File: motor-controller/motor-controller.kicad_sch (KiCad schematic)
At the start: 14 parts, among them Q1 IRFZ44, Q2 IRFZ44, Q3 IRFZ44, Q4 IRFZ44, Q5 VN2222L, Q6 VN2222L, U1 MCT6, U2 LT1161

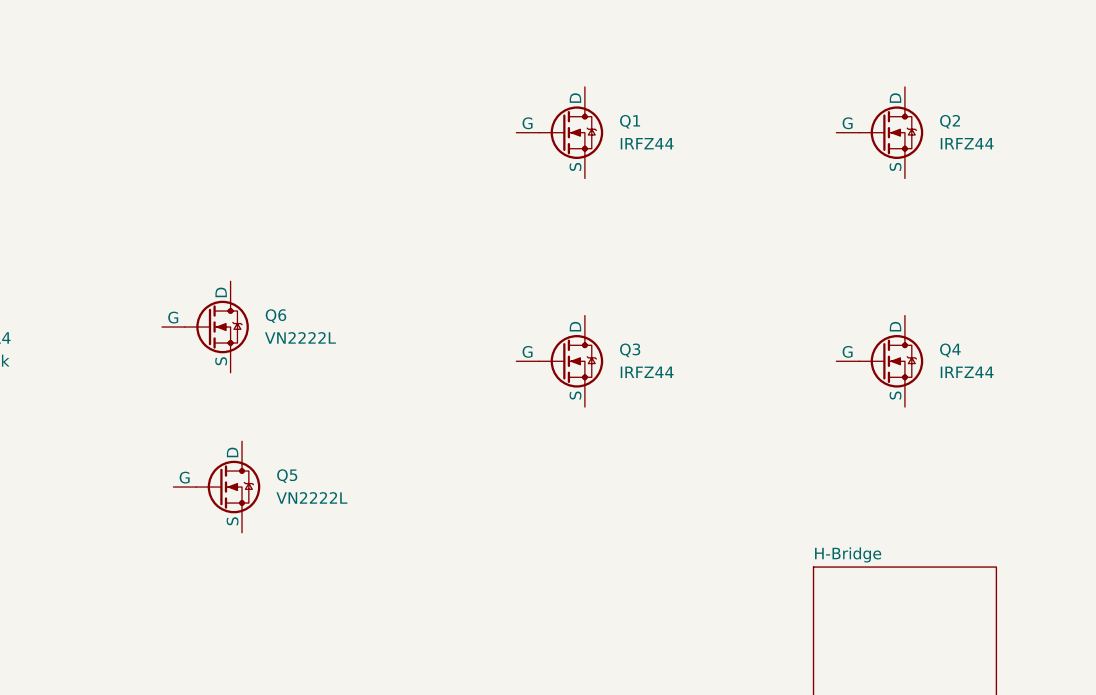
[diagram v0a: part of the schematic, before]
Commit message: Create H-Bridge schematic
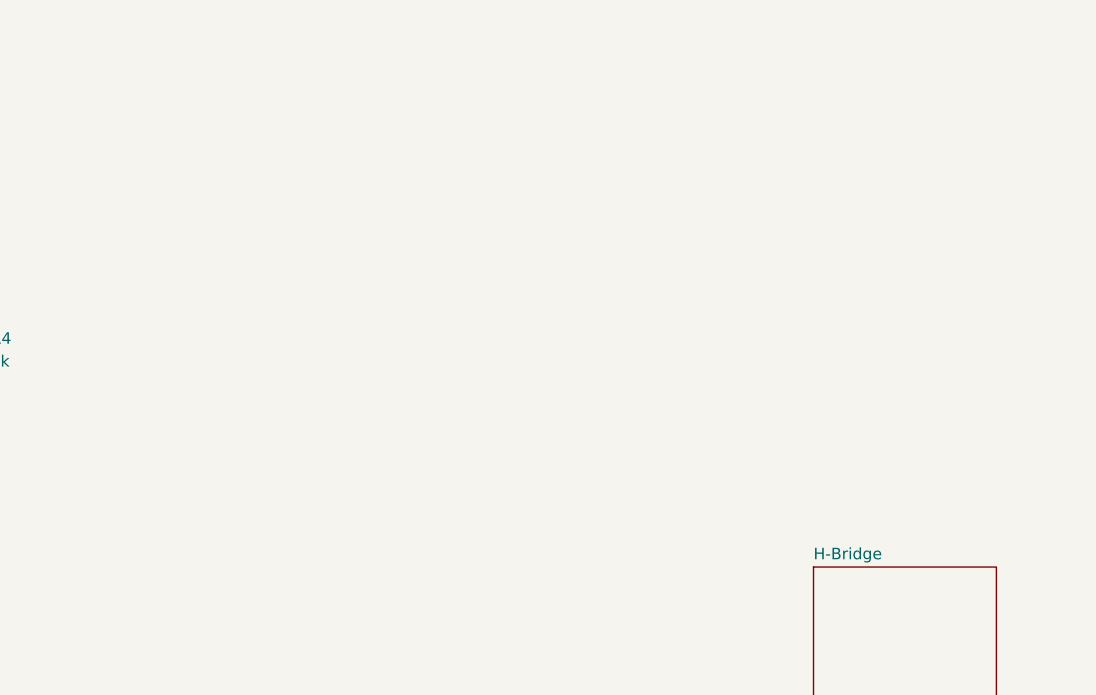
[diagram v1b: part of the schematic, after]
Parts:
- removed Q1, Q2, Q3, Q4: IRFZ44, Package_TO_SOT_THT:TO-220-3_Vertical, symbol GS_Transistors:MOSFET_N-Ch_60V_48A_23mR
- removed Q5, Q6: VN2222L, Package_TO_SOT_THT:TO-92_Inline, symbol GS_Transistors:MOSFET_N-Ch_60V_0.23A_7500mR
- C1, C2: symbol Device:C -> GS_Capacitor_THT:C_THT_100nF
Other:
- company: (none) -> Team 5

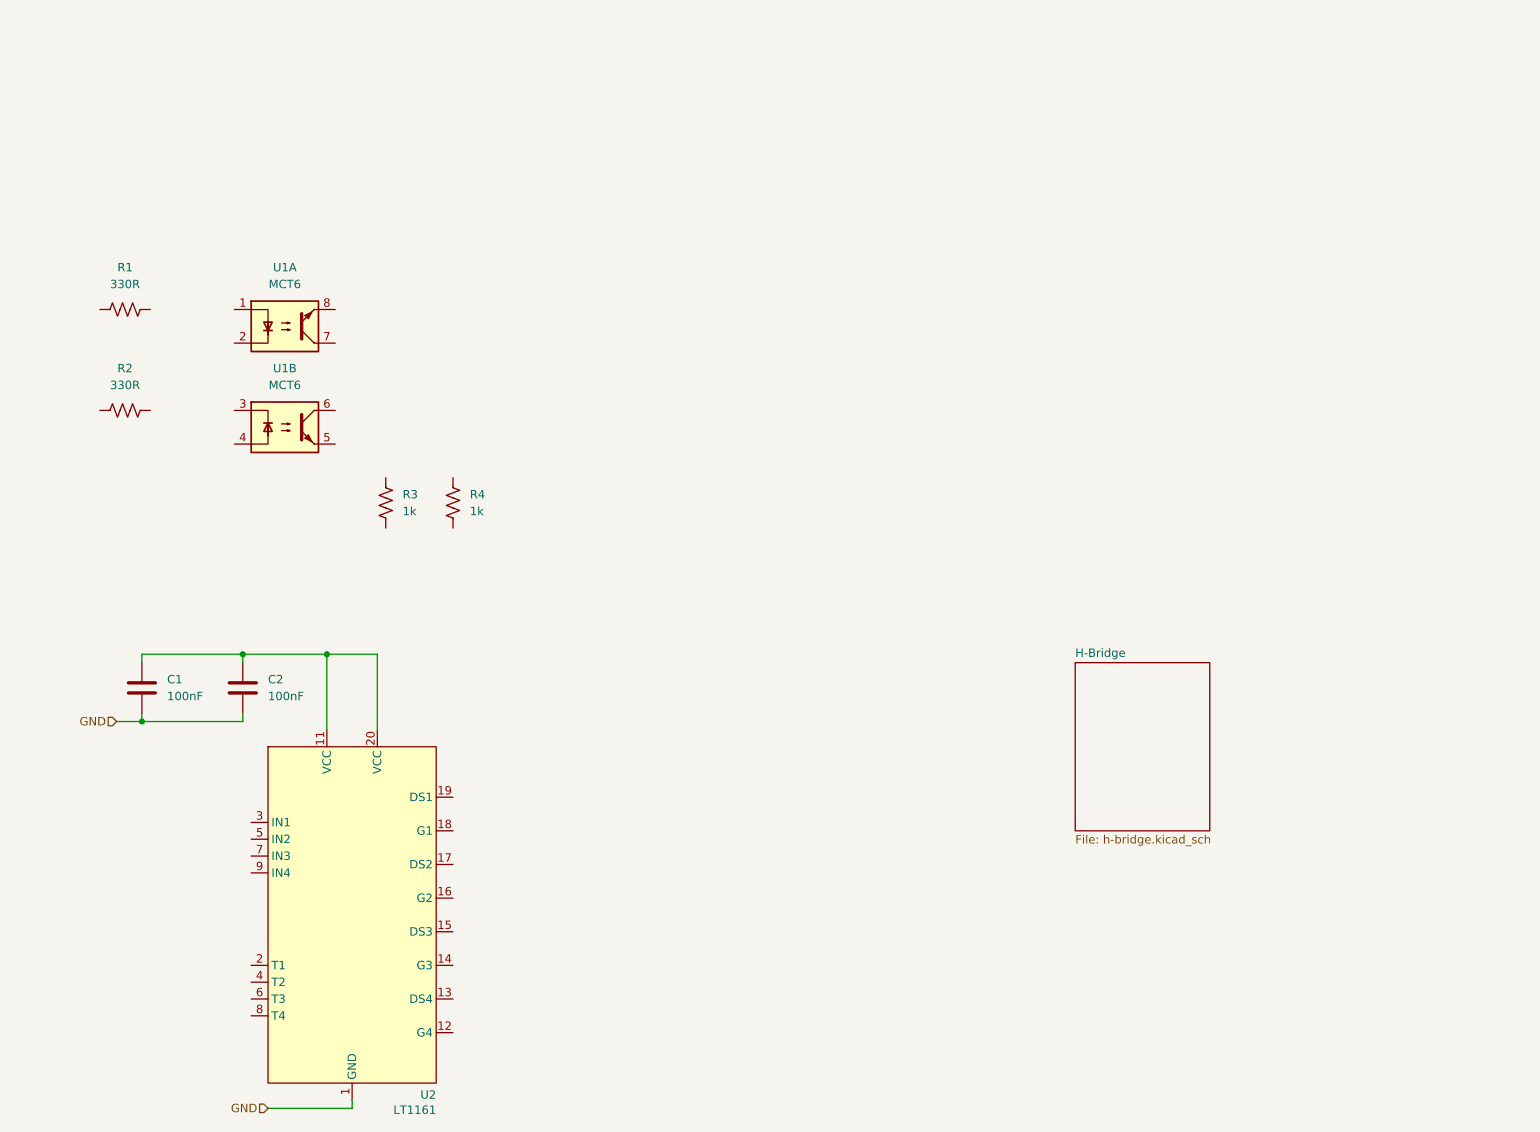
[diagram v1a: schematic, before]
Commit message: Finish optocoupler and gate-driver
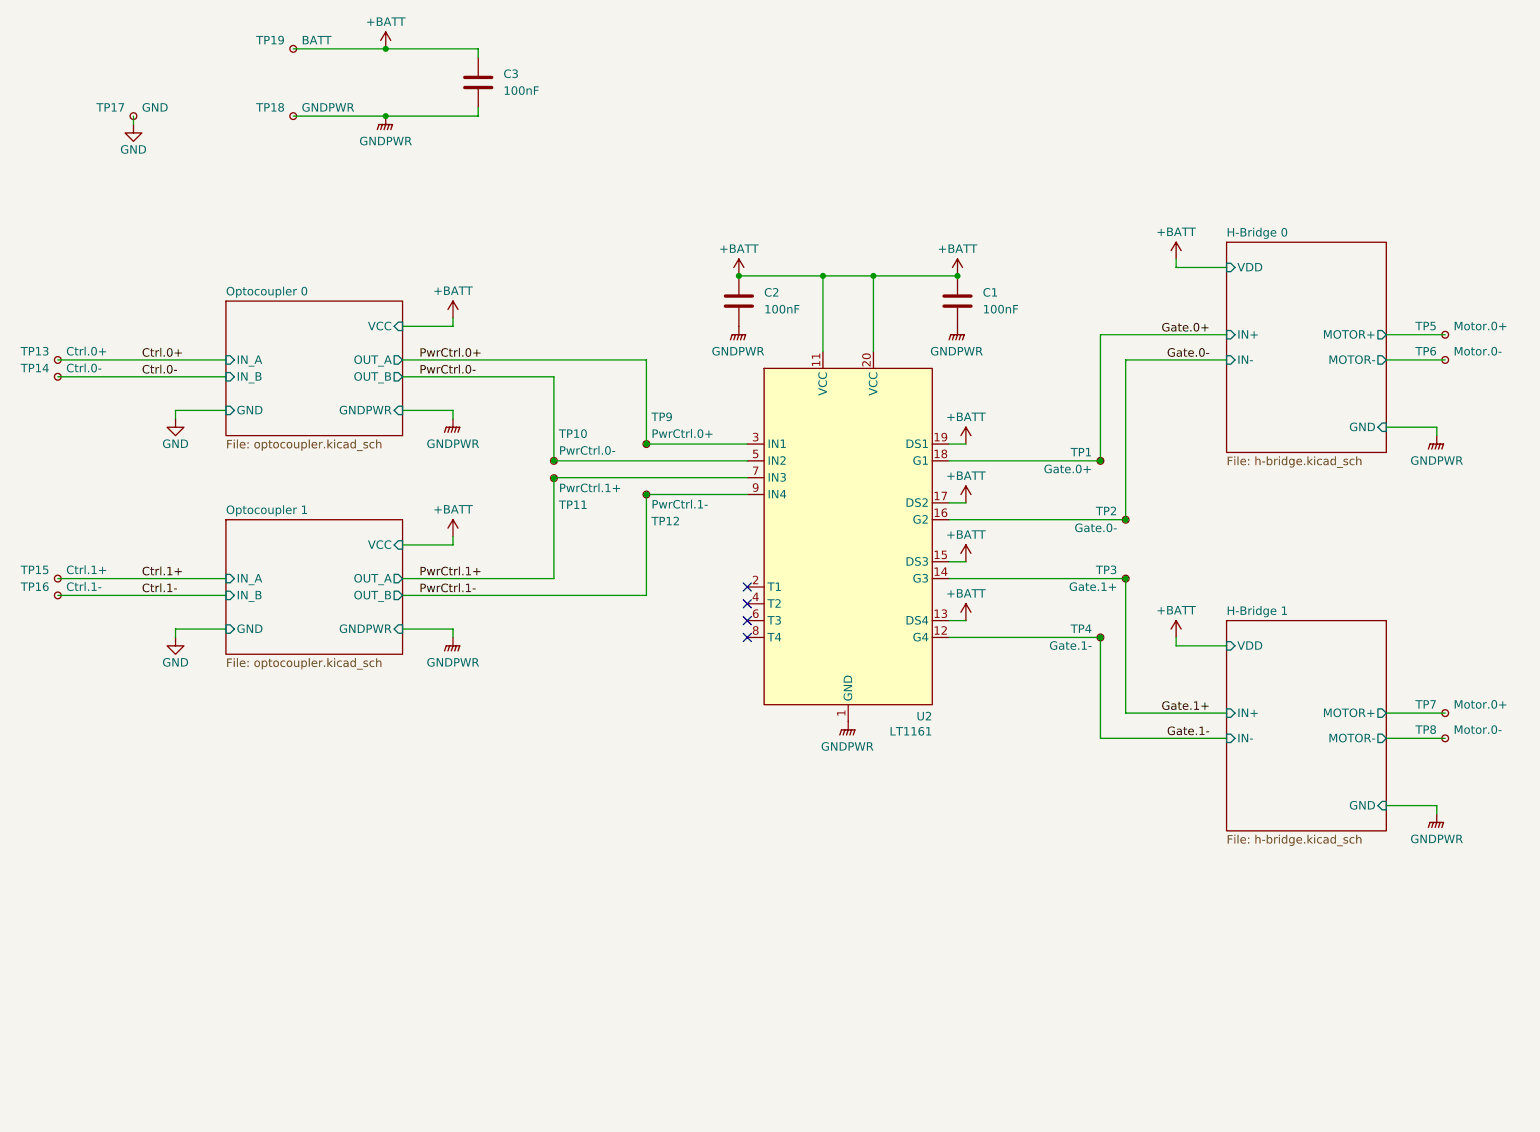
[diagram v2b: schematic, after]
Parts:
- removed R1, R2: 330R, Resistor_THT:R_Axial_DIN0309_L9.0mm_D3.2mm_P12.70mm_Horizontal, symbol Device:R_US
- removed R3, R4: 1k, Resistor_THT:R_Axial_DIN0309_L9.0mm_D3.2mm_P12.70mm_Horizontal, symbol Device:R_US
- removed U1: MCT6, Package_DIP:DIP-8_W7.62mm_LongPads, symbol GS_Optoelectronic:MCT6
- added C3: 100nF, Capacitor_THT:C_Disc_D3.0mm_W2.0mm_P2.50mm, symbol GS_Capacitor_THT:C_THT_100nF
- added TP1: Gate.0+, TestPoint:TestPoint_Pad_1.5x1.5mm, symbol Connector:TestPoint_Small
- added TP10: PwrCtrl.0-, TestPoint:TestPoint_Pad_1.5x1.5mm, symbol Connector:TestPoint_Small
- added TP11: PwrCtrl.1+, TestPoint:TestPoint_Pad_1.5x1.5mm, symbol Connector:TestPoint_Small
- added TP12: PwrCtrl.1-, TestPoint:TestPoint_Pad_1.5x1.5mm, symbol Connector:TestPoint_Small
- added TP13: Ctrl.0+, TestPoint:TestPoint_Pad_1.5x1.5mm, symbol Connector:TestPoint_Small
- added TP14: Ctrl.0-, TestPoint:TestPoint_Pad_1.5x1.5mm, symbol Connector:TestPoint_Small
- added TP15: Ctrl.1+, TestPoint:TestPoint_Pad_1.5x1.5mm, symbol Connector:TestPoint_Small
- added TP16: Ctrl.1-, TestPoint:TestPoint_Pad_1.5x1.5mm, symbol Connector:TestPoint_Small
- added TP17: GND, TestPoint:TestPoint_Pad_1.5x1.5mm, symbol Connector:TestPoint_Small
- added TP18: GNDPWR, TestPoint:TestPoint_Pad_1.5x1.5mm, symbol Connector:TestPoint_Small
- added TP19: BATT, TestPoint:TestPoint_Pad_1.5x1.5mm, symbol Connector:TestPoint_Small
- added TP2: Gate.0-, TestPoint:TestPoint_Pad_1.5x1.5mm, symbol Connector:TestPoint_Small
- added TP3: Gate.1+, TestPoint:TestPoint_Pad_1.5x1.5mm, symbol Connector:TestPoint_Small
- added TP4: Gate.1-, TestPoint:TestPoint_Pad_1.5x1.5mm, symbol Connector:TestPoint_Small
- added TP5, TP7: Motor.0+, TestPoint:TestPoint_Pad_1.5x1.5mm, symbol Connector:TestPoint_Small
- added TP6, TP8: Motor.0-, TestPoint:TestPoint_Pad_1.5x1.5mm, symbol Connector:TestPoint_Small
- added TP9: PwrCtrl.0+, TestPoint:TestPoint_Pad_1.5x1.5mm, symbol Connector:TestPoint_Small
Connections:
- net GND: now also C3.2, TP17.1, TP18.1
- net +BATT: now reaches C1.1, C2.1, U2.11 (VCC), U2.20 (VCC)
- net +BATT: now also U2.13 (DS4), U2.15 (DS3), U2.17 (DS2), U2.19 (DS1), C3.1, TP19.1
- net Gate.1-: now reaches U2.12 (G4)
- net Gate.1-: now also TP4.1
- net Gate.1+: now reaches U2.14 (G3)
- net Gate.1+: now also TP3.1
- net Gate.0-: now reaches U2.16 (G2)
- net Gate.0-: now also TP2.1
- net Gate.0+: now reaches U2.18 (G1)
- net Gate.0+: now also TP1.1
- net PwrCtrl.0+: now reaches U2.3 (IN1)
- net PwrCtrl.0+: now also TP9.1
- net PwrCtrl.0-: now reaches U2.5 (IN2)
- net PwrCtrl.0-: now also TP10.1
- net PwrCtrl.1+: now reaches U2.7 (IN3)
- net PwrCtrl.1+: now also TP11.1
- net PwrCtrl.1-: now reaches U2.9 (IN4)
- net PwrCtrl.1-: now also TP12.1
- new net Ctrl.0+: TP13.1
- new net Ctrl.0-: TP14.1
- new net Ctrl.1+: TP15.1
- new net Ctrl.1-: TP16.1
- new net H-Bridge 0/MOTOR+: TP5.1
- new net H-Bridge 0/MOTOR-: TP6.1
- new net H-Bridge 1/MOTOR+: TP7.1
- new net H-Bridge 1/MOTOR-: TP8.1
- no-connect marks 0 -> 4
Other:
- sheet H-Bridge renamed H-Bridge 1
- added sheet H-Bridge 0 (h-bridge.kicad_sch)
- added sheet Optocoupler 0 (optocoupler.kicad_sch)
- added sheet Optocoupler 1 (optocoupler.kicad_sch)
- sheet H-Bridge 1 ports: added GND, IN+, IN-, MOTOR+, MOTOR-, VDD; removed none
- title: (none) -> Motor Controller
- moved on the sheet: C1, C2, U2

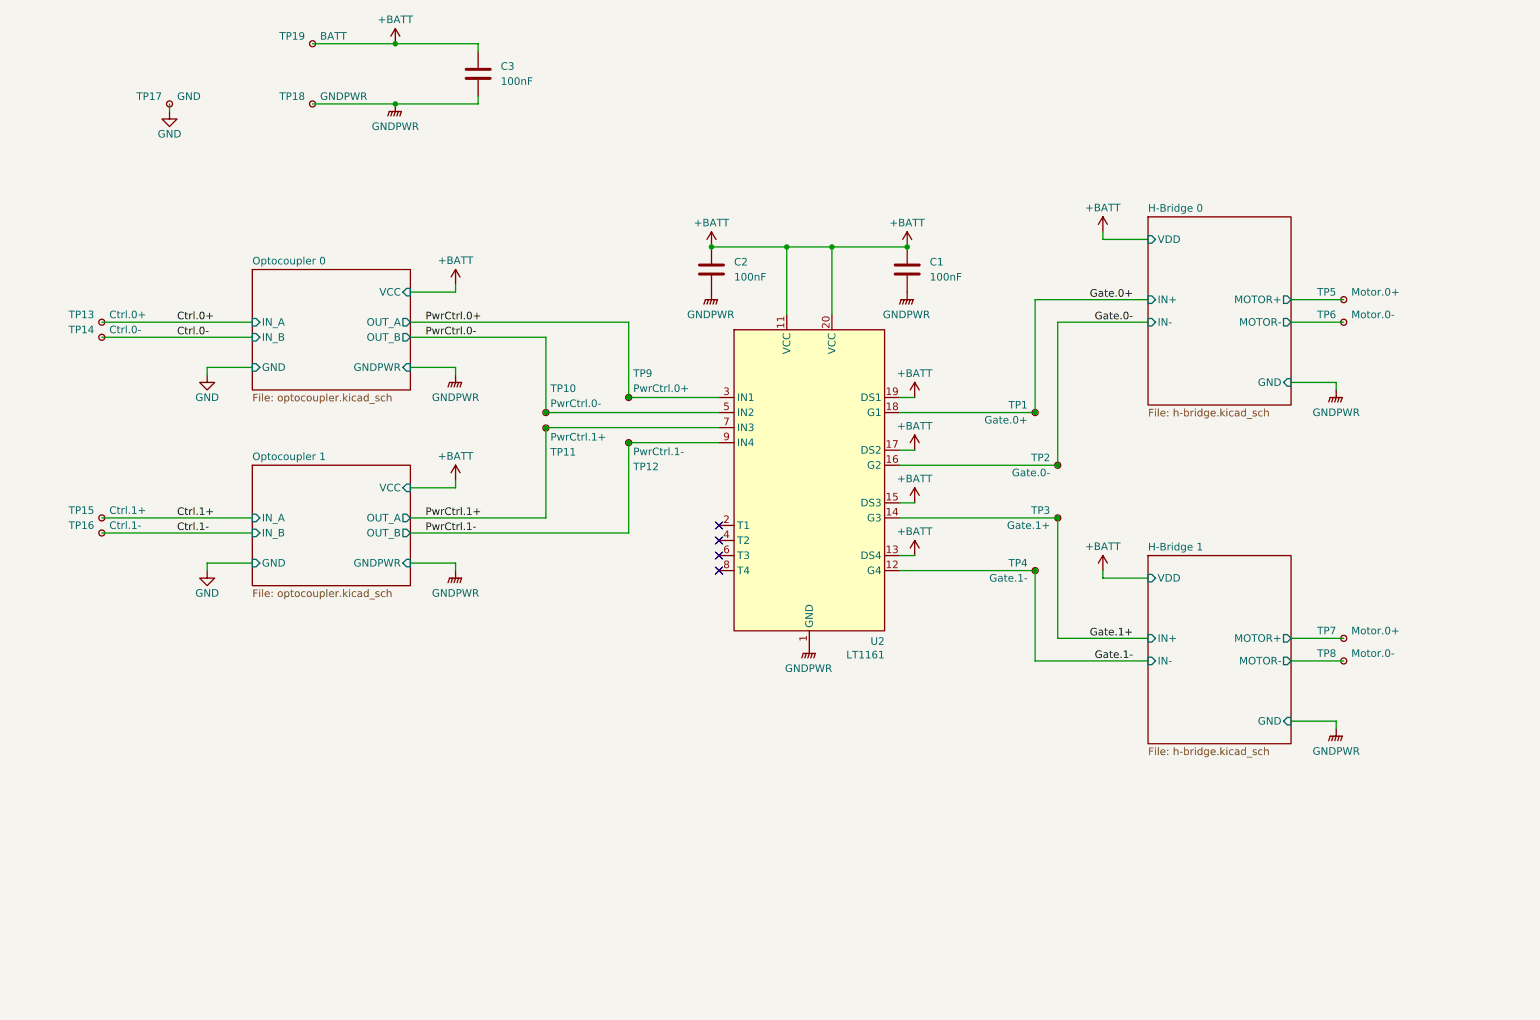
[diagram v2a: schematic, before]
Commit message: Finish H-Bridge schematic
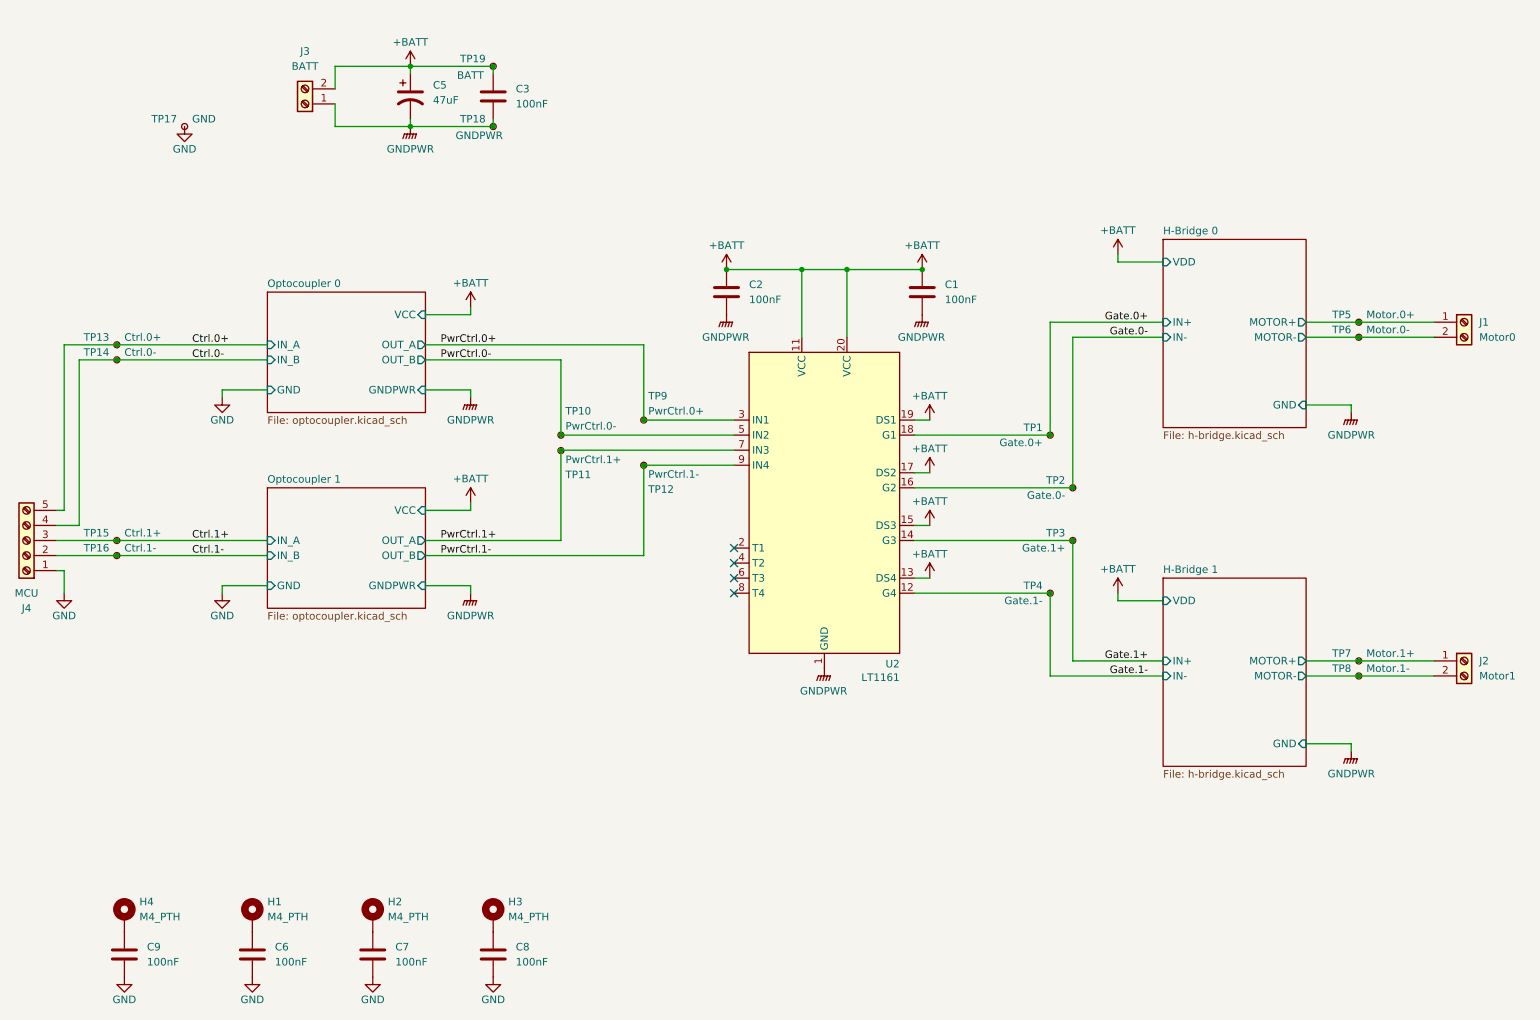
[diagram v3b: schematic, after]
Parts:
- added C5: 47uF, Capacitor_THT:C_Radial_D5.0mm_H11.0mm_P2.00mm, symbol Device:C_Polarized_US
- added C6, C7, C8, C9: 100nF, Capacitor_THT:C_Disc_D3.0mm_W2.0mm_P2.50mm, symbol GS_Capacitor_THT:C_THT_100nF
- added H1, H2, H3, H4: M4_PTH, MountingHole:MountingHole_4.3mm_M4_Pad, symbol Mechanical:MountingHole_Pad
- added J1: Motor0, TerminalBlock:TerminalBlock_MaiXu_MX126-5.0-02P_1x02_P5.00mm, symbol Connector:Screw_Terminal_01x02
- added J2: Motor1, TerminalBlock:TerminalBlock_MaiXu_MX126-5.0-02P_1x02_P5.00mm, symbol Connector:Screw_Terminal_01x02
- added J3: BATT, TerminalBlock:TerminalBlock_MaiXu_MX126-5.0-02P_1x02_P5.00mm, symbol Connector:Screw_Terminal_01x02
- added J4: MCU, TerminalBlock:TerminalBlock_Xinya_XY308-2.54-5P_1x05_P2.54mm_Horizontal, symbol Connector:Screw_Terminal_01x05
- TP7: value Motor.0+ -> Motor.1+
- TP8: value Motor.0- -> Motor.1-
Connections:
- net +BATT: now also C5.1, J3.2 (Pin_2)
- net Ctrl.0+: now also J4.5 (Pin_5)
- net Ctrl.0-: now also J4.4 (Pin_4)
- net Ctrl.1+: now also J4.3 (Pin_3)
- net Ctrl.1-: now also J4.2 (Pin_2)
- net GND: now also C5.2, C6.2, C7.2, C8.2, C9.2, J3.1 (Pin_1), J4.1 (Pin_1)
- net H-Bridge 0/MOTOR+: now also J1.1 (Pin_1)
- net H-Bridge 0/MOTOR-: now also J1.2 (Pin_2)
- net H-Bridge 1/MOTOR+: now also J2.1 (Pin_1)
- net H-Bridge 1/MOTOR-: now also J2.2 (Pin_2)
- new net: C8.1, H3.1
- new net: C6.1, H1.1
- new net: C7.1, H2.1
- new net: C9.1, H4.1
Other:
- moved on the sheet: C1, C2, C3, TP1, TP10, TP11, TP12, TP13, TP14, TP15, TP16, TP17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
